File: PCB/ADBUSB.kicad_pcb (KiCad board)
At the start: 2 copper layers, 36.2 x 36 mm, 6 parts, among them J1 MLD-MDC-4-02, J2 MLD-MDC-4-02, SW1 SW_Slide_DPDT SHOU HAN MSK-22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, U1 ProMicro

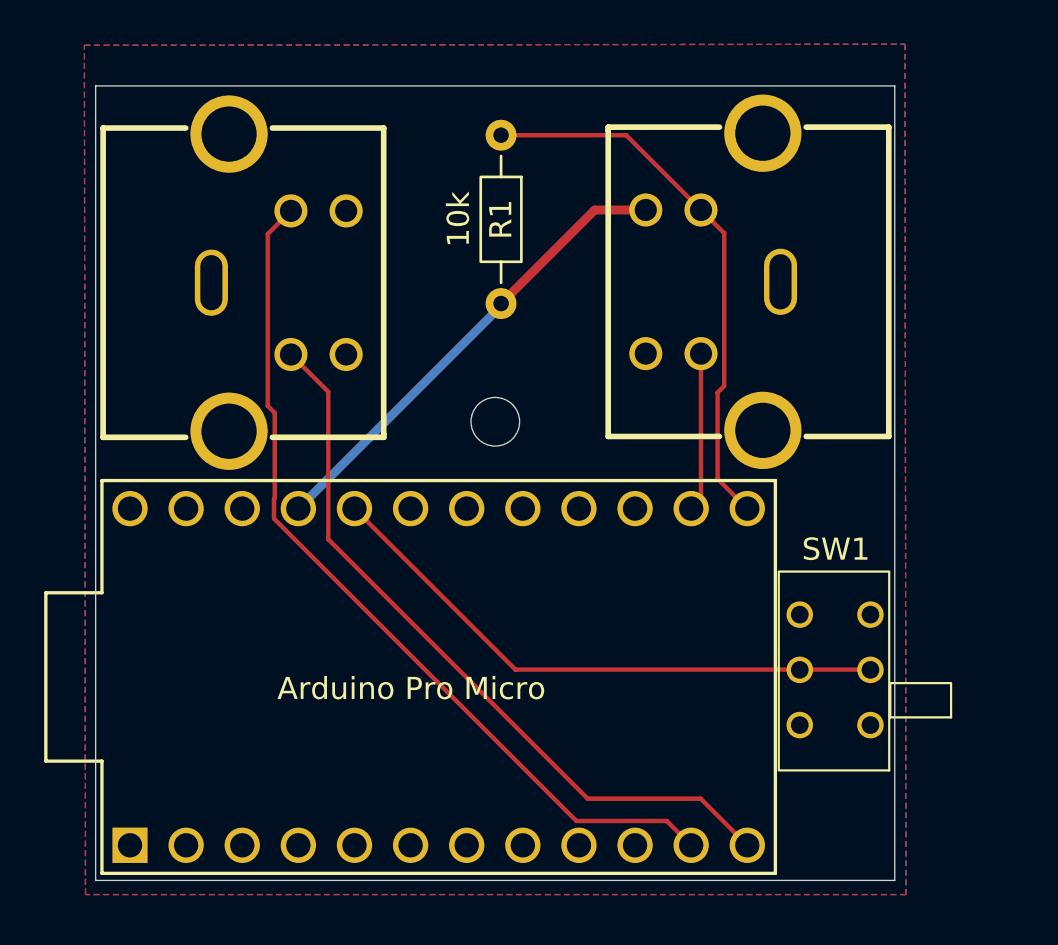
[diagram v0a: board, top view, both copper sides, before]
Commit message: Update for diode, pushbutton, raw
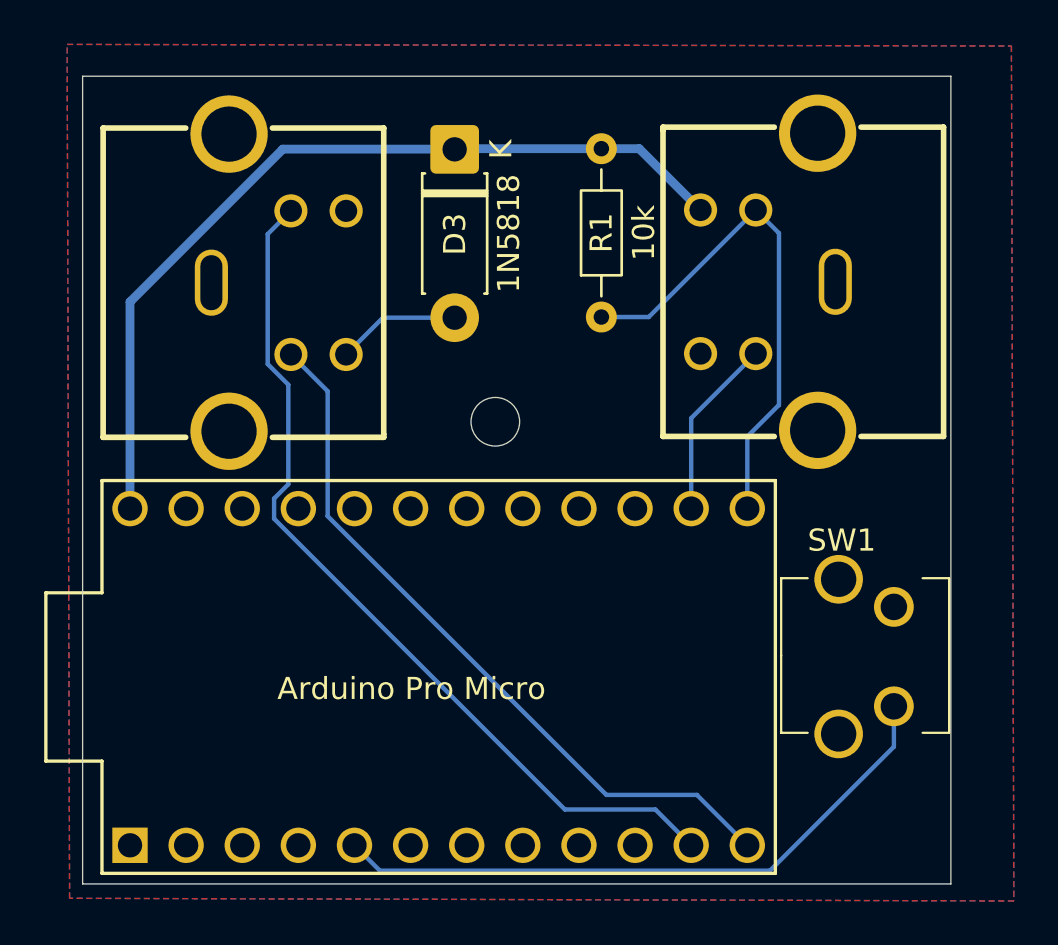
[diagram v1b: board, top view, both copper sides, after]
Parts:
- added D3: 1N5818, Diode_THT:D_DO-41_SOD81_P7.62mm_Horizontal, F.Cu at (154.4, 63.8)
- SW1: value SW_Slide_DPDT SHOU HAN MSK-22D18G4 051 -> SW_SPST; footprint DIN5:DPDT slide switch C7507433 -> Pushbutton:SPST_power_switch
- moved R1 9.40 mm to (161.1, 71.4), turned to 90 degrees
- moved SW1 3.48 mm to (171.8, 86.7), turned to 90 degrees
- moved J2 2.48 mm to (171.5, 69.6)
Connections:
- J1 pad 3: unconnected-(J1-Pad3) -> Net-(D3-A)
- J2 pad 3: VCC -> RAW_5V
- R1 pad 2: VCC -> RAW_5V
- SW1 pad 1: GND -> Net-(U1-SDA)
- SW1 pad 2: Net-(U1-F4) -> GND
- SW1 pad 3: unconnected-(SW1-C-Pad3) -> GND
- SW1 pad 4: unconnected-(SW1-A-Pad4) -> GND
- U1 pad 20: Net-(U1-F4) -> unconnected-(U1-F4-Pad20)
- U1 pad 21: VCC -> unconnected-(U1-VCC-Pad21)
- U1 pad 24: unconnected-(U1-RAW-Pad24) -> RAW_5V
- U1 pad 5: unconnected-(U1-SDA-Pad5) -> Net-(U1-SDA)
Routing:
- net RAW_5V: track 0.00 -> 39.2 mm
- net Net-(U1-SDA): track 0.00 -> 29.0 mm
- net Net-(U1-F4): track 26.4 -> 0.00 mm
- net VCC: track 21.4 -> 0.00 mm
- net Net-(D3-A): track 0.00 -> 5.60 mm
- net Net-(U1-B6): track 25.1 -> 23.5 mm
- net Net-(U1-B2): track 7.20 -> 8.23 mm
- net Net-(U1-B5): track 34.1 -> 33.5 mm
- net Net-(U1-B4): track 39.9 -> 40.4 mm
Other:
- board size 36.2 x 36 mm -> 39.3 x 36.6 mm
